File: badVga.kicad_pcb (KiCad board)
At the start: 4 copper layers, 114.5 x 94.1 mm, 35 parts, among them SW1 SW_DIP_x04, U1 27C010, U10 74HC244, U11 CD74HC4040, U12 74LS20, U13 74LS20, U14 74LS30, U15 74LS30, U16 74LS00, U17 CD74HC4040, U18 74LS30, U19 74LS30, U2 74HC245, U20 74LS00, U3 74LS00, U4 74LS32, U5 74HC14, U6 M48Zx2, U7 74HC245, U8 74HC245, U9 74HC245, Y1 TFT660

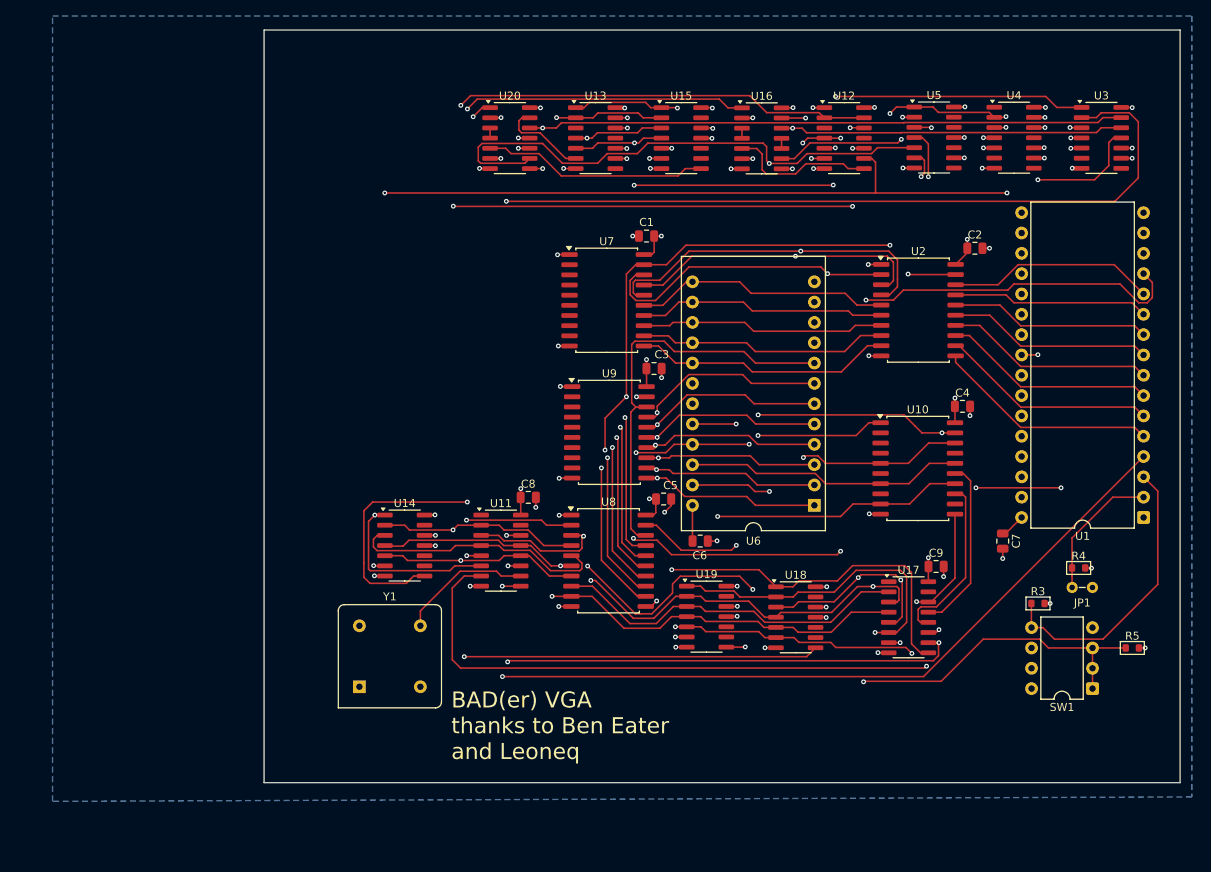
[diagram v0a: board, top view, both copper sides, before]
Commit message: adjust to sbc6309 io
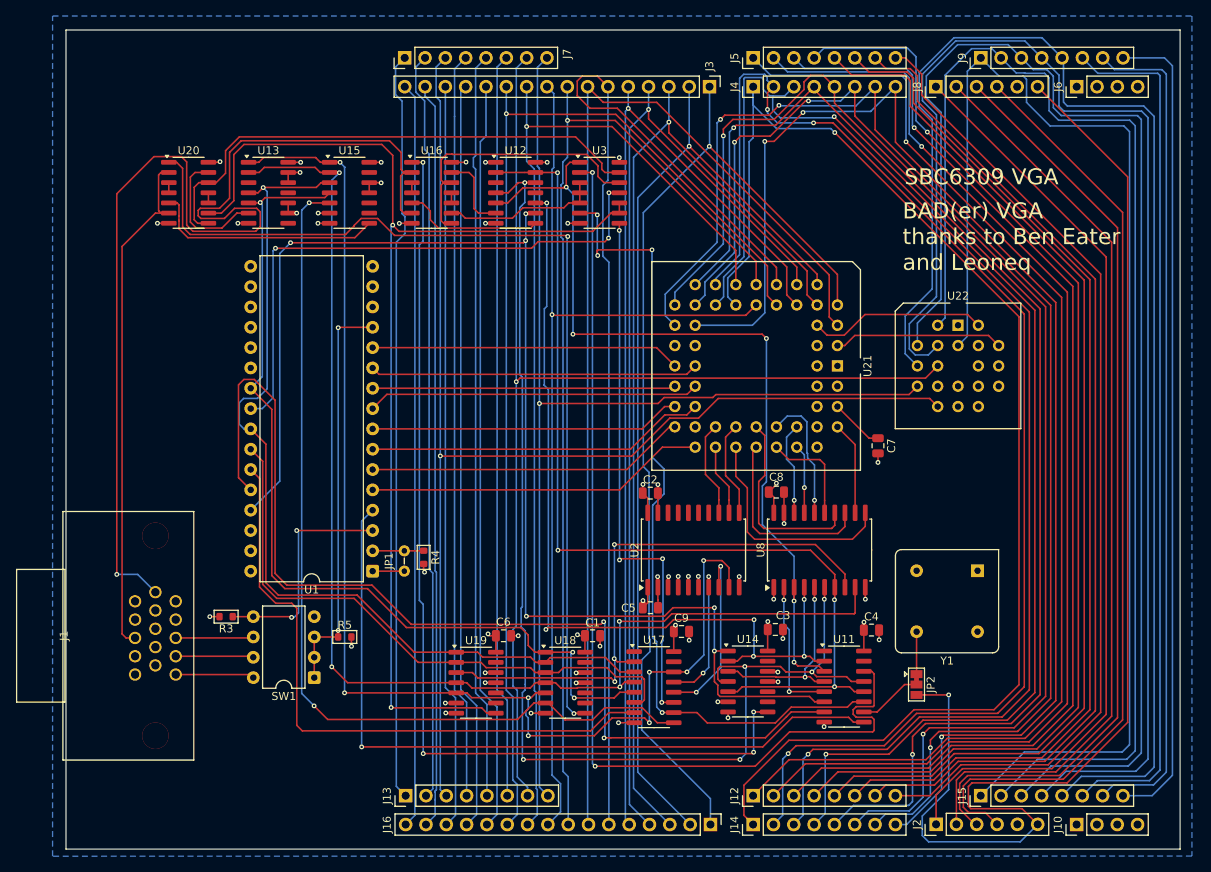
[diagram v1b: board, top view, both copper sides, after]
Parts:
- removed U10: 74HC244, Package_SO:SOIC-20W_7.5x12.8mm_P1.27mm
- removed U4: 74LS32, Package_SO:SOIC-14_3.9x8.7mm_P1.27mm
- removed U5: 74HC14, Package_SO:SOIC-14_3.9x8.7mm_P1.27mm
- removed U6: M48Zx2, Package_DIP:DIP-24_18.0mmx34.29mm_W15.24mm
- removed U7, U9: 74HC245, Package_SO:SOIC-20W_7.5x12.8mm_P1.27mm
- added J1: VGA, Library:CONN_AHDF15A-KG-TAXB_ASM, F.Cu at (82.5, 128.0)
- added J10: Conn_01x04, Connector_PinHeader_2.54mm:PinHeader_1x04_P2.54mm_Vertical, F.Cu at (209.1, 151.6)
- added J12: Conn_01x08, Connector_PinHeader_2.54mm:PinHeader_1x08_P2.54mm_Vertical, F.Cu at (168.7, 148.0)
- added J13: Conn_01x08, Connector_PinHeader_2.54mm:PinHeader_1x08_P2.54mm_Vertical, F.Cu at (125.2, 148.0)
- added J14: Conn_01x08, Connector_PinHeader_2.54mm:PinHeader_1x08_P2.54mm_Vertical, F.Cu at (168.7, 151.6)
- added J15: Conn_01x08, Connector_PinHeader_2.54mm:PinHeader_1x08_P2.54mm_Vertical, F.Cu at (197.1, 148.0)
- added J16: Conn_01x16, Connector_PinHeader_2.54mm:PinHeader_1x16_P2.54mm_Vertical, F.Cu at (163.3, 151.6)
- added J2: Conn_01x06, Connector_PinHeader_2.54mm:PinHeader_1x06_P2.54mm_Vertical, F.Cu at (191.5, 151.5)
- added J3: Conn_01x16, Connector_PinHeader_2.54mm:PinHeader_1x16_P2.54mm_Vertical, F.Cu at (163.2, 59.3)
- added J4: Conn_01x08, Connector_PinHeader_2.54mm:PinHeader_1x08_P2.54mm_Vertical, F.Cu at (168.7, 59.3)
- added J5: Conn_01x08, Connector_PinHeader_2.54mm:PinHeader_1x08_P2.54mm_Vertical, F.Cu at (168.7, 55.7)
- added J6: Conn_01x04, Connector_PinHeader_2.54mm:PinHeader_1x04_P2.54mm_Vertical, F.Cu at (209.1, 59.3)
- added J7: Conn_01x08, Connector_PinHeader_2.54mm:PinHeader_1x08_P2.54mm_Vertical, F.Cu at (125.1, 55.7)
- added J8: Conn_01x06, Connector_PinHeader_2.54mm:PinHeader_1x06_P2.54mm_Vertical, F.Cu at (191.5, 59.3)
- added J9: Conn_01x08, Connector_PinHeader_2.54mm:PinHeader_1x08_P2.54mm_Vertical, F.Cu at (197.1, 55.7)
- added JP2: videoclock source, Jumper:SolderJumper-3_P1.3mm_Bridged12_Pad1.0x1.5mm, F.Cu at (189.1, 134.1)
- added U21: IDT71342, Package_LCC:PLCC-52_THT-Socket, F.Cu at (179.2, 94.2)
- added U22: GAL16V8, Package_LCC:PLCC-20_THT-Socket, F.Cu at (194.3, 89.2)
- moved R3 101.5 mm to (102.8, 125.6), turned to 180 degrees
- moved R5 98.5 mm to (117.6, 128.1)
- moved SW1 97.3 mm to (113.8, 133.2)
- moved U1 96.6 mm to (121.1, 119.9)
- moved JP1 86.0 mm to (125.1, 119.9), turned to 90 degrees
- moved R4 81.9 mm to (127.5, 118.2), turned to -90 degrees
- moved Y1 78.6 mm to (196.7, 119.8), turned to 180 degrees
- moved U3 63.1 mm to (149.5, 72.6)
- moved C2 50.8 mm to (155.8, 110.1)
- moved C1 50.4 mm to (148.6, 128.0), turned to 0 degrees
- moved U14 46.1 mm to (168.0, 133.7)
- moved U11 46.1 mm to (180.0, 134.3)
- moved U15 42.0 mm to (118.2, 72.6)
- moved U16 41.8 mm to (128.5, 72.6)
- moved U12 41.6 mm to (139.0, 72.6)
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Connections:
- net Net-(U1-D0) renamed /pixel
- U1 pad 10: Net-(U1-A2) -> D2
- U1 pad 11: Net-(U1-A1) -> D1
- U1 pad 12: Net-(U1-A0) -> D0
- U1 pad 5: Net-(U1-A7) -> D7
- U1 pad 6: Net-(U1-A6) -> D6
- U1 pad 7: Net-(U1-A5) -> D5
- U1 pad 8: Net-(U1-A4) -> D4
- U1 pad 9: Net-(U1-A3) -> D3
- U18 pad 1: VB0 -> VB3
- U18 pad 2: VB2 -> VB4
- U18 pad 3: VB3 -> VB2
- U18 pad 4: VB4 -> VB6
- U18 pad 5: VB6 -> VB9
- U18 pad 6: VB9 -> VB0
- U19 pad 1: VB2 -> VB4
- U19 pad 2: VB4 -> VB2
- U2 pad 11: Net-(U1-A7) -> A10
- U2 pad 12: Net-(U1-A6) -> A9
- U2 pad 13: Net-(U1-A5) -> A8
- U2 pad 14: Net-(U1-A4) -> unconnected-(U2-B4-Pad14)
- U2 pad 15: Net-(U1-A3) -> unconnected-(U2-B3-Pad15)
- U2 pad 16: Net-(U1-A2) -> unconnected-(U2-B2-Pad16)
- U2 pad 17: Net-(U1-A1) -> unconnected-(U2-B1-Pad17)
- U2 pad 18: Net-(U1-A0) -> unconnected-(U2-B0-Pad18)
- U2 pad 19: ~{RD} -> GND
- U2 pad 2: D0 -> GND
- U2 pad 3: D1 -> GND
- U2 pad 4: D2 -> GND
- U2 pad 5: D3 -> GND
- U2 pad 6: D4 -> GND
- U2 pad 7: D5 -> VB7
- U2 pad 8: D6 -> VB8
- U2 pad 9: D7 -> VB9
- U3 pad 10: GND -> Net-(U19-Pad8)
- U3 pad 4: GND -> Net-(U16-Pad9)
- U3 pad 5: GND -> Net-(U16-Pad9)
- U3 pad 6: unconnected-(U3-Pad6) -> VCLK
- U3 pad 8: unconnected-(U3-Pad8) -> RST
- U3 pad 9: GND -> Net-(U19-Pad8)
- U8 pad 19: ~{RD} -> GND
- Y1 pad 5: CLK -> Net-(JP2-A)
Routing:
- net DEV3: track 0.00 -> 172.4 mm
- net DEV4: track 0.00 -> 172.1 mm
- net DX2: track 0.00 -> 170.5 mm, vias 0 -> 2
- net DX6: track 0.00 -> 168.3 mm, vias 0 -> 3
- net DX1: track 0.00 -> 167.7 mm, vias 0 -> 3
- net DEV2: track 0.00 -> 166.8 mm
- net DX0: track 0.00 -> 166.5 mm, vias 0 -> 1
- net DX4: track 0.00 -> 166.2 mm, vias 0 -> 2
- net DX7: track 0.00 -> 165.3 mm, vias 0 -> 3
- net DX5: track 0.00 -> 161.5 mm, vias 0 -> 3
- net DEV1: track 0.00 -> 160.4 mm
- net DX3: track 0.00 -> 159.7 mm, vias 0 -> 2
- net DEV0: track 0.00 -> 159.1 mm
- net R/~{W}: track 0.00 -> 158.8 mm, vias 0 -> 1
- net CLK24: track 0.00 -> 158.1 mm, vias 0 -> 1
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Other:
- board size 114.5 x 94.1 mm -> 139.3 x 102.4 mm
- board text added: "SBC6309 VGA"

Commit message: improve rom use
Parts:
- removed JP1: ZWORKA, PCM_Jumper_AKL:Jumper_P2.54mm_D0.7mm
- added R1: 10K, PCM_Resistor_SMD_AKL:R_0603_1608Metric, F.Cu at (104.7, 141.8)
- added R10: 20K, PCM_Resistor_SMD_AKL:R_0603_1608Metric, F.Cu at (102.3, 86.9)
- added R11: 20K, PCM_Resistor_SMD_AKL:R_0603_1608Metric, F.Cu at (102.3, 91.9)
- added R12: 100K, PCM_Resistor_SMD_AKL:R_0603_1608Metric, F.Cu at (96.3, 81.8)
- added R13: 100K, PCM_Resistor_SMD_AKL:R_0603_1608Metric, F.Cu at (96.3, 87.0)
- added R14: 100K, PCM_Resistor_SMD_AKL:R_0603_1608Metric, F.Cu at (96.3, 92.3)
- added R15: 10K, PCM_Resistor_SMD_AKL:R_0603_1608Metric, F.Cu at (106.0, 147.8)
- added R16: 10K, PCM_Resistor_SMD_AKL:R_0603_1608Metric, F.Cu at (106.0, 150.3)
- added R17: 1K, PCM_Resistor_SMD_AKL:R_0603_1608Metric, F.Cu at (96.3, 80.1)
- added R18: 1K, PCM_Resistor_SMD_AKL:R_0603_1608Metric, F.Cu at (96.3, 83.5)
- added R19: 1K, PCM_Resistor_SMD_AKL:R_0603_1608Metric, F.Cu at (96.3, 85.3)
- added R2: 10K, PCM_Resistor_SMD_AKL:R_0603_1608Metric, F.Cu at (106.0, 145.2)
- added R20: 1K, PCM_Resistor_SMD_AKL:R_0603_1608Metric, F.Cu at (96.3, 88.8)
- added R21: 1K, PCM_Resistor_SMD_AKL:R_0603_1608Metric, F.Cu at (96.3, 90.6)
- added R22: 1K, PCM_Resistor_SMD_AKL:R_0603_1608Metric, F.Cu at (96.3, 94.1)
- added R23: 75R, PCM_Resistor_SMD_AKL:R_0603_1608Metric, F.Cu at (103.4, 127.7)
- added R24: 75R, PCM_Resistor_SMD_AKL:R_0603_1608Metric, F.Cu at (106.3, 130.8)
- added R25: 75R, PCM_Resistor_SMD_AKL:R_0603_1608Metric, F.Cu at (103.4, 133.5)
- added R6: 10K, PCM_Resistor_SMD_AKL:R_0603_1608Metric, F.Cu at (102.3, 79.4)
- added R7: 10K, PCM_Resistor_SMD_AKL:R_0603_1608Metric, F.Cu at (102.3, 84.3)
- added R8: 10K, PCM_Resistor_SMD_AKL:R_0603_1608Metric, F.Cu at (102.3, 89.4)
- added R9: 20K, PCM_Resistor_SMD_AKL:R_0603_1608Metric, F.Cu at (102.3, 81.8)
- added U10: 74LVC1G3157, Package_SON:Texas_USON-6_1x1.45mm_P0.5mm_SMD, F.Cu at (109.5, 126.5)
- added U23: 74LVC1G3157, Package_SON:Texas_USON-6_1x1.45mm_P0.5mm_SMD, F.Cu at (113.0, 130.9)
- added U24: 74LVC1G3157, Package_SON:Texas_USON-6_1x1.45mm_P0.5mm_SMD, F.Cu at (113.0, 127.9)
- added U25: 74LVC1G3157, Package_SON:Texas_USON-6_1x1.45mm_P0.5mm_SMD, F.Cu at (113.0, 125.2)
- added U7: 74LVC1G3157, Package_SON:Texas_USON-6_1x1.45mm_P0.5mm_SMD, F.Cu at (109.5, 132.4)
- added U9: 74LVC1G3157, Package_SON:Texas_USON-6_1x1.45mm_P0.5mm_SMD, F.Cu at (109.5, 129.3)
- added Y2: TFT660, Oscillator:Oscillator_DIP-14, F.Cu at (189.1, 112.2)
- J1: footprint Library:CONN_AHDF15A-KG-TAXB_ASM -> Connector_Dsub:DSUB-15-HD_Socket_Horizontal_P2.29x2.54mm_EdgePinOffset8.35mm_Housed_MountingHolesOffset10.89mm
- SW1: value SW_DIP_x04 -> SW_DIP_x06; footprint Package_DIP:DIP-8_W7.62mm -> Button_Switch_THT:SW_DIP_SPSTx06_Slide_6.7x16.8mm_W7.62mm_P2.54mm_LowProfile
- U12, U13: value 74LS20 -> 74HCT20
- U16, U20, U3: value 74LS00 -> 74HCT00
- U2, U8: value 74HC245 -> 74HCT245
- moved R5 40.3 mm to (125.2, 88.6), turned to 90 degrees
- moved J1 17.6 mm to (99.5, 132.3), turned to -90 degrees
- moved SW1 17.3 mm to (116.8, 150.3)
- moved R3 16.7 mm to (106.7, 141.8), turned to 90 degrees
- moved Y1 10.8 mm to (189.1, 112.2), turned to -90 degrees
- moved R4 2.41 mm to (125.1, 118.2)
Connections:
- J1 pad 1: RED -> xRED
- J1 pad 2: GREEN -> xGREEN
- J1 pad 3: BLUE -> xBLUE
- SW1 pad 1: /pixel -> +5V
- SW1 pad 2: /pixel -> +5V
- SW1 pad 3: /pixel -> +5V
- SW1 pad 5: INV -> +5V
- SW1 pad 6: BLUE -> +5V
- SW1 pad 7: GREEN -> CP438
- SW1 pad 8: RED -> COLOUR
- U1 pad 15: unconnected-(U1-D2-Pad15) -> Net-(U1-D2)
- U1 pad 17: unconnected-(U1-D3-Pad17) -> Net-(U1-D3)
- U1 pad 18: unconnected-(U1-D4-Pad18) -> Net-(U1-D4)
- U1 pad 19: unconnected-(U1-D5-Pad19) -> Net-(U1-D5)
- U1 pad 20: unconnected-(U1-D6-Pad20) -> Net-(U1-D6)
- U1 pad 21: unconnected-(U1-D7-Pad21) -> Net-(U1-D7)
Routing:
- net RED2: track 0.00 -> 73.3 mm, vias 0 -> 2
- net GREEN2: track 0.00 -> 65.2 mm, vias 0 -> 2
- net BLUE2: track 0.00 -> 56.8 mm, vias 0 -> 2
- net CP438: track 6.38 -> 42.6 mm, vias 0 -> 2
- net Net-(U1-D2): track 0.00 -> 27.1 mm
- net COLOUR: track 0.00 -> 26.1 mm, vias 0 -> 3
- net RED: track 9.86 -> 30.3 mm, vias 0 -> 1
- net GREEN: track 9.75 -> 29.6 mm, vias 0 -> 1
- net /pixel: track 51.1 -> 70.1 mm, vias 2 -> 1
- net BLUE: track 9.75 -> 27.8 mm, vias 0 -> 1
- net INV: track 28.5 -> 44.4 mm, vias 2 -> 1
- net GND: track 49.9 -> 65.6 mm, vias 31 -> 54
- net Net-(JP2-A): track 5.31 -> 17.5 mm
- net Net-(U1-D4): track 0.00 -> 10.5 mm
- net Net-(U1-D6): track 0.00 -> 10.1 mm
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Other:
- board size 139.3 x 102.4 mm -> 132.3 x 102.4 mm
- board text added: "B"
- board text added: "COLOUR"
- board text added: "FONT"
- board text added: "G"
- board text added: "INV"
- board text added: "R"

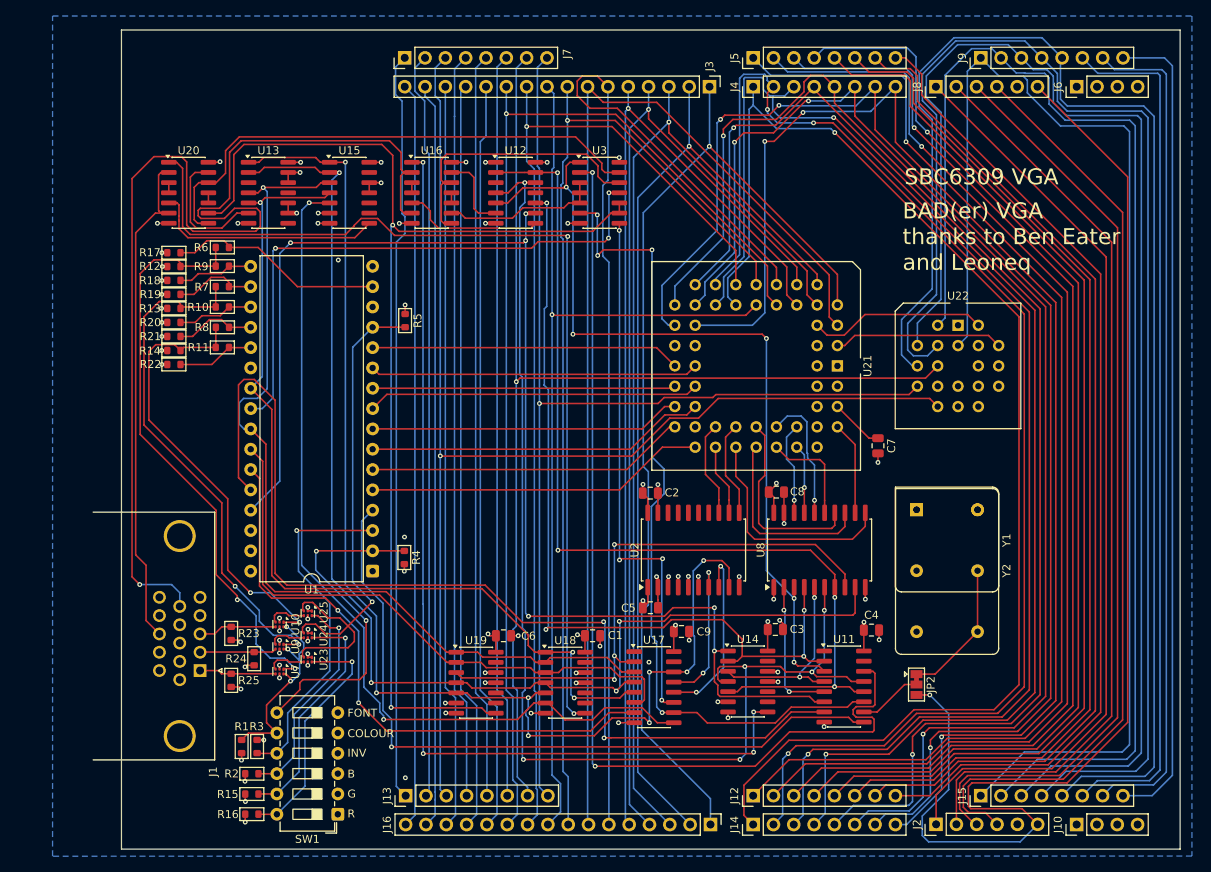
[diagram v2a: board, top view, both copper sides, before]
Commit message: fix sync signals
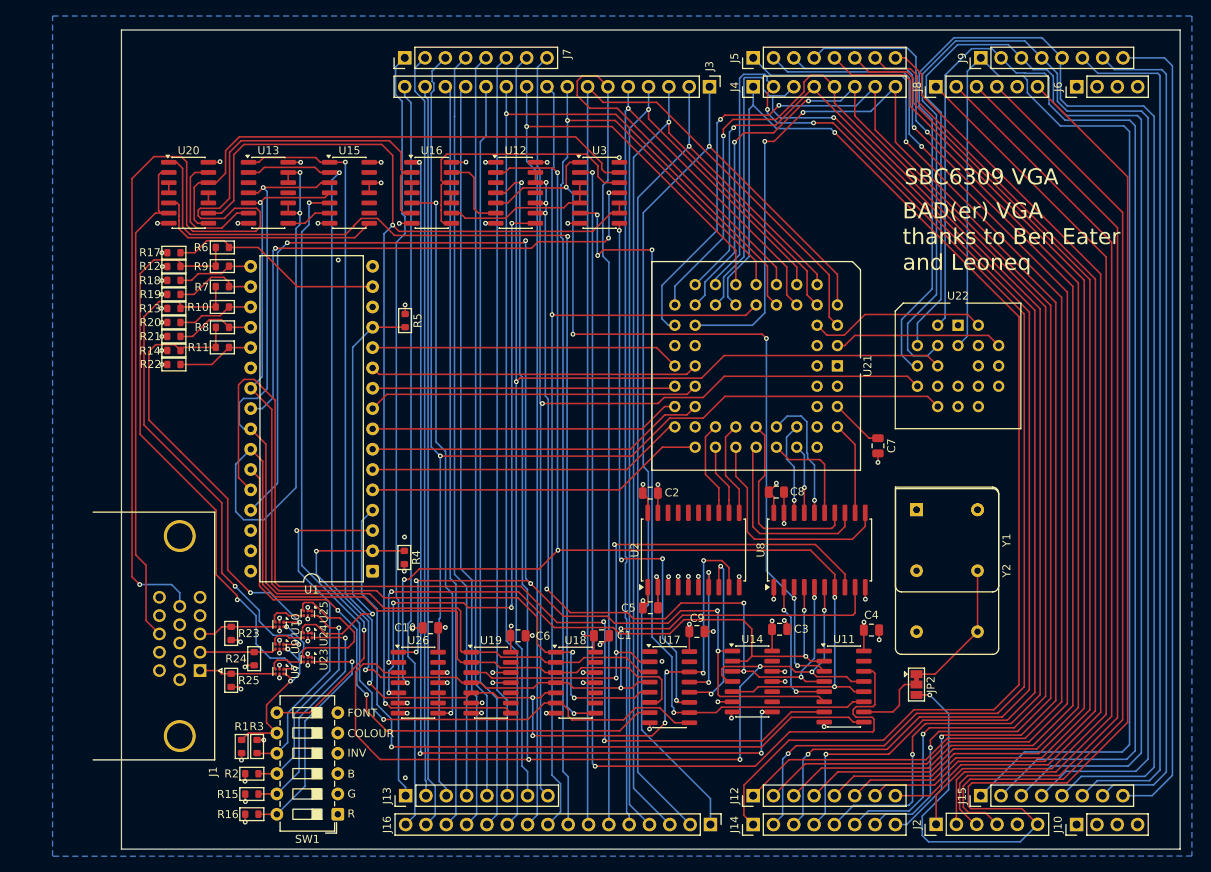
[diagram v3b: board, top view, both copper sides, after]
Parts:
- added C10: 10nF, Capacitor_SMD:C_0805_2012Metric, F.Cu at (128.3, 127.0)
- added U26: 74LS30, Package_SO:SOIC-14_3.9x8.7mm_P1.27mm, F.Cu at (126.8, 133.8)
- moved U17 1.96 mm to (158.2, 134.4)
- moved C9 1.93 mm to (161.6, 127.4)
- moved U19 1.87 mm to (135.9, 133.8)
- moved C6 1.82 mm to (139.3, 128.0)
- moved U18 1.28 mm to (146.5, 133.8)
- moved C1 1.12 mm to (149.7, 128.0)
- moved U14 0.56 mm to (168.6, 133.7)
- moved C3 0.53 mm to (172.0, 127.2)
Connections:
- U12 pad 10: HB2 -> HB3
- U12 pad 12: HB4 -> HB3
- U12 pad 13: HB5 -> HB3
- U12 pad 9: HB12 -> HB3
- U13 pad 10: GND -> VB2
- U13 pad 12: GND -> VB2
- U13 pad 13: GND -> VB2
- U13 pad 8: unconnected-(U13-Pad8) -> Net-(U13-Pad8)
- U13 pad 9: GND -> VB2
- U15 pad 6: +5V -> Net-(U13-Pad8)
- U16 pad 5: Net-(U12-Pad8) -> Net-(U16-Pad5)
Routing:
- net HB3: track 24.5 -> 116.3 mm, vias 2 -> 8
- net Net-(U16-Pad5): track 0.00 -> 69.3 mm, vias 0 -> 2
- net VB2: track 74.6 -> 143.6 mm, vias 0 -> 2
- net Net-(U12-Pad8): track 17.6 -> 78.7 mm, vias 0 -> 4
- net HB5: track 122.3 -> 157.9 mm, vias 4 -> 6
- net HB4: track 150.5 -> 184.3 mm
- net HB2: track 104.6 -> 83.4 mm
- net HB12: track 166.8 -> 185.6 mm, vias 6 -> 7
- net +5V: track 66.0 -> 77.2 mm, vias 35 -> 38
- net Net-(U13-Pad8): track 0.00 -> 5.71 mm
- net VB4: track 115.7 -> 120.6 mm
- net GND: track 65.6 -> 61.4 mm
- net VB3: track 115.2 -> 119.0 mm
- net VCLK: track 101.0 -> 97.8 mm
- net Net-(U19-Pad8): track 143.9 -> 146.6 mm
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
